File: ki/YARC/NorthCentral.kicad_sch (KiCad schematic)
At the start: 10 parts, among them U102 74HC245, U103 74HC245, U106 74LS139, U128 74LS157, U132 74LS157, U133 74LS21, U134 74LS32, U138 74LS14

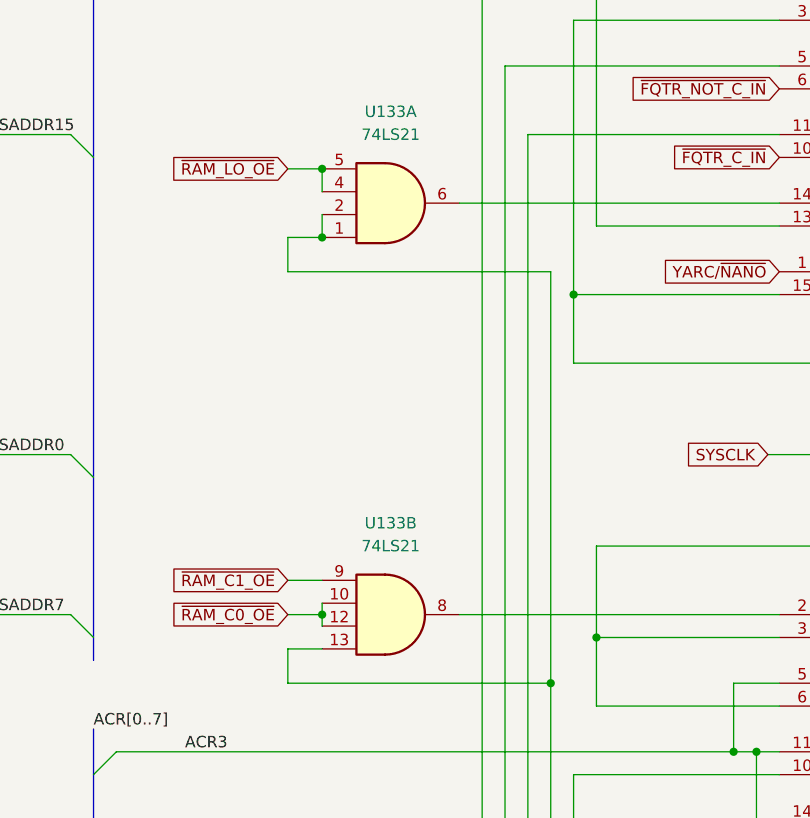
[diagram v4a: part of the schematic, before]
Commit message: Convert schematic to KiCad 7
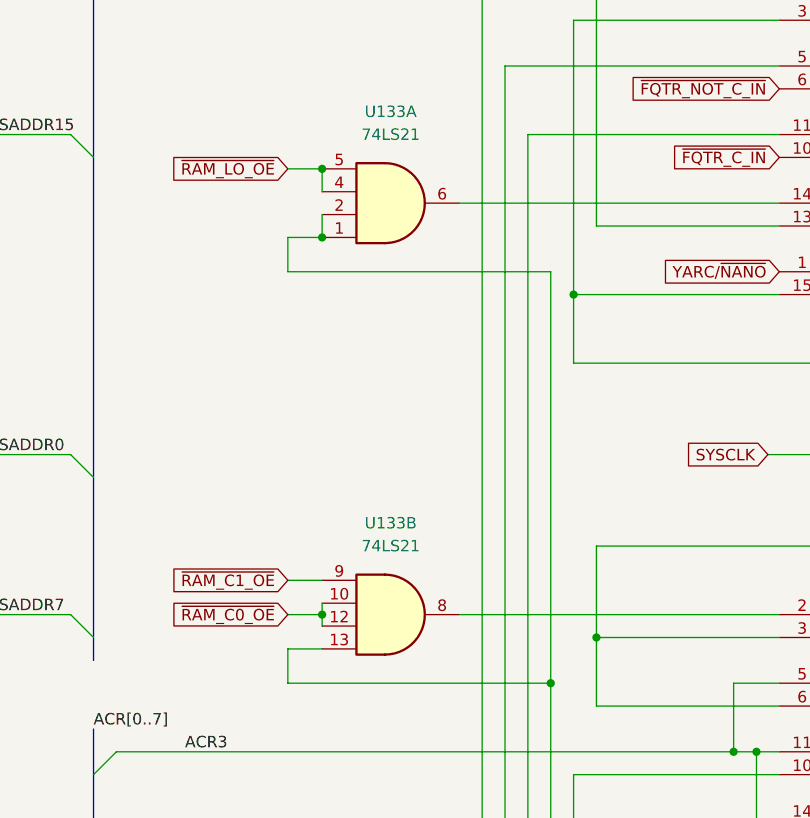
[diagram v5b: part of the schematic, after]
